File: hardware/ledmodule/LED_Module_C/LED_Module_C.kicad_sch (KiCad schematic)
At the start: 99 parts, among them J1 Conn_01x02, J10 Conn_01x02, J11 Conn_01x02, J12 Conn_01x02, J13 Conn_01x02, J14 Conn_01x02, J15 Conn_01x02, J16 Conn_01x02, J17 Conn_01x02, J18 Conn_01x02, J19 Conn_01x02, J2 Conn_01x02, J20 Conn_01x02, J21 Conn_01x02, J22 Conn_01x02, J23 Conn_01x02, J24 Conn_01x02, J25 Conn_01x02, J26 Conn_01x04_Pin, J3 Conn_01x02, J4 Conn_01x02, J5 Conn_01x02, J6 Conn_01x02, J7 Conn_01x02, J8 Conn_01x02, J9 Conn_01x02, U1 TMP1075DSG

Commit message: Apply open hardware licenses.
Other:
- title: (none) -> besteLampe! LED Moudule C
- moved on the sheet: AC0, AC1, AC2, AD0, AD1, AD2, AH0, AH1, AH2, AL0, AL1, AL2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

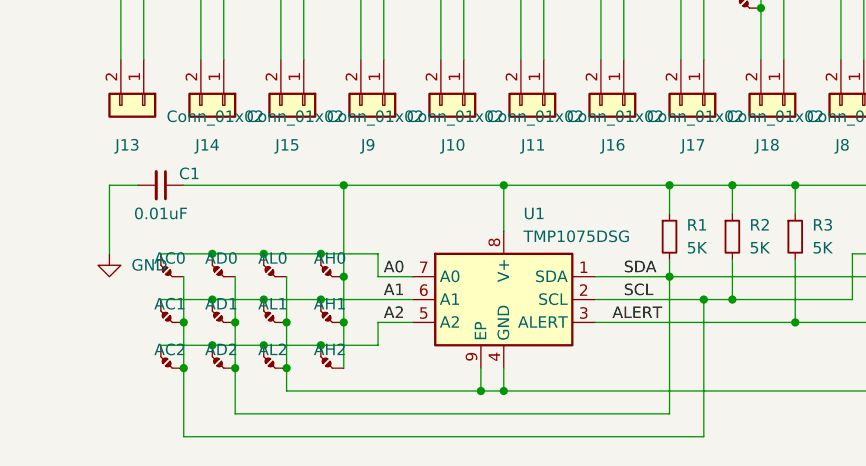
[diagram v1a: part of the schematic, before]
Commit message: Several changes to LED modules A2 and C, two items added to the library. Readme updated.
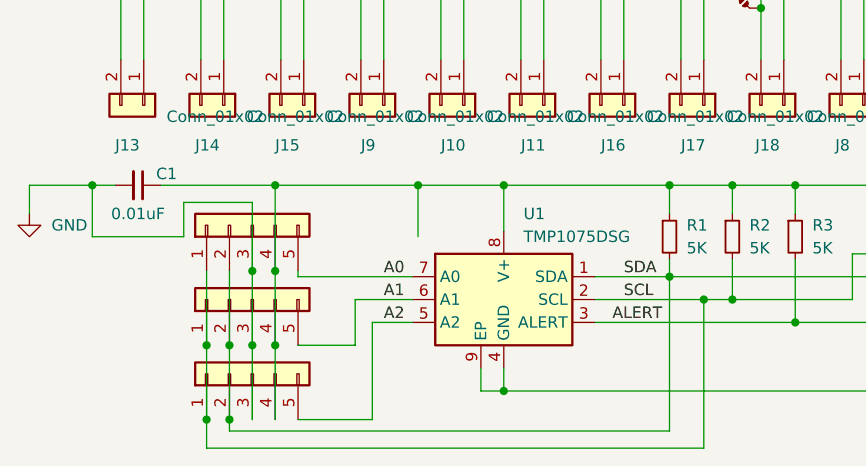
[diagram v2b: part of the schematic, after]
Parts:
- removed AC0, AC1, AC2, AD0, AD1, AD2, AH0, AH1, AH2, AL0, AL1, AL2: ~, Jumper:SolderJumper-2_P1.3mm_Open_RoundedPad1.0x1.5mm, symbol Connector:Diagonal_Solder_Jumper
- added J27, J28, J29: Conn_01x05, Jumper:Quadforce, symbol Connector_Generic:Conn_01x05
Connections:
- net +3.3V: now also J27.4 (Pin_4), J28.4 (Pin_4), J29.4 (Pin_4)
- net A0: now also J27.5 (Pin_5)
- net A1: now also J28.5 (Pin_5)
- net A2: now also J29.5 (Pin_5)
- net GND: now also J27.3 (Pin_3), J28.3 (Pin_3), J29.3 (Pin_3)
- net SCL: now also J27.1 (Pin_1), J28.1 (Pin_1), J29.1 (Pin_1)
- net SDA: now also J27.2 (Pin_2), J28.2 (Pin_2), J29.2 (Pin_2)
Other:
- moved on the sheet: C1
